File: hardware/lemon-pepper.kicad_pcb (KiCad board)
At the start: 2 copper layers, 42 x 42 mm, 124 parts, among them J101 INPUT, J201 USB_C_Receptacle_USB2.0, J301 DEBUG, M101 MOT, Q501 AO3400A, Q701 CMSA30N06T, Q702 CMSA30N06T, Q703 CMSA30N06T, SW301 RESET, SW302 USER, U201 SRV05-4, U301 STM32G431, U302 SN65HVD230, U401 MT6835, U501 FD6288, U601 MAX17504ATP+T, U602 XC6206, U801 CC6900SO-5A, U802 CC6900SO-5A, U803 CC6900SO-5A, Y301 12MHz

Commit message: try new driver
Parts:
- removed C307: 20p, Capacitor_SMD:C_0402_1005Metric
- removed C504: 470n, Capacitor_SMD:C_0805_2012Metric
- removed C603, C604: 10u, Capacitor_SMD:C_0805_2012Metric
- removed C605, C801, C802, C803: 100n, Capacitor_SMD:C_0402_1005Metric
- removed C606: 2u2, Capacitor_SMD:C_0805_2012Metric
- removed C607: 12n, Capacitor_SMD:C_0402_1005Metric
- removed C608, C609: 22uF, Capacitor_SMD:C_0805_2012Metric
- removed D503: SS210, Diode_SMD:D_SMA
- removed L601: 4u7, Inductor_SMD:L_Vishay_IHLP-4040
- removed NT601: NET TIE, NetTie:NetTie-2_SMD_Pad2.0mm
- removed Q701, Q702, Q703: CMSA30N06T, easyeda2kicad:DFN-8_L5.5-W5.2-P1.27-LS6.0-BL-EP2
- removed R303, R304, R701, R704, R705, R708, R709, R712, R713, R714, R715: 22R, Resistor_SMD:R_0402_1005Metric
- removed R305, R702, R703, R706, R707, R710, R711, R804, R805, R806: 10k, Resistor_SMD:R_0402_1005Metric
- removed R602: 100k, Resistor_SMD:R_0402_1005Metric
- removed R603: 22k, Resistor_SMD:R_0402_1005Metric
- removed R801, R802, R803: 20k, Resistor_SMD:R_0402_1005Metric
- removed SW301: RESET, matei:TS-1187A-B-A-B
- removed TP601: Vmot, TestPoint:TestPoint_Pad_D1.0mm
- removed TP602: 5V, TestPoint:TestPoint_Pad_D1.0mm
- removed TP603: 3V3, TestPoint:TestPoint_Pad_D1.0mm
- removed U602: XC6206, Package_TO_SOT_SMD:SOT-23
- removed U801, U802, U803: CC6900SO-5A, easyeda2kicad:SOP-8_L4.9-W3.9-P1.27-LS6.0-BL
- added C109: 100uF, Capacitor_SMD:CP_Elec_10x10.5, F.Cu at (86.6, 38.8)
- added C110: 100uF, Capacitor_SMD:CP_Elec_10x10.5, F.Cu at (86.6, 50.9)
- added C111: 100uF, Capacitor_SMD:CP_Elec_10x10.5, F.Cu at (86.6, 62.9)
- added C112: 100uF, Capacitor_SMD:CP_Elec_10x10.5, F.Cu at (86.6, 75.0)
- added D101: SS210, Diode_SMD:D_SMA, F.Cu at (161.9, 84.8)
- added D601: OCD, Diode_SMD:D_0603_1608Metric, F.Cu at (159.3, 87.4)
- added D602: 1N4148WS, Diode_SMD:D_SOD-323, F.Cu at (159.4, 91.9)
- added D603: 1N4148WS, Diode_SMD:D_SOD-323, F.Cu at (159.4, 89.9)
- added L501: 33u, Inductor_SMD:L_1210_3225Metric, F.Cu at (160.8, 94.5)
- added R502: 51k, Resistor_SMD:R_0402_1005Metric, F.Cu at (155.7, 96.8)
- added R503: 22k, Resistor_SMD:R_0402_1005Metric, F.Cu at (154.6, 96.8)
- added R504: 5R, Resistor_SMD:R_0603_1608Metric, F.Cu at (161.8, 79.0)
- added R505: 15k, Resistor_SMD:R_0402_1005Metric, F.Cu at (156.2, 80.0)
- added U701: ACS711KEXLT-31AB-T, easyeda2kicad:IC-SMD_ACS711KEXLT-15AB-T, F.Cu at (141.6, 78.1)
- added U702: ACS711KEXLT-31AB-T, easyeda2kicad:IC-SMD_ACS711KEXLT-15AB-T, F.Cu at (150.9, 78.1)
- added U703: ACS711KEXLT-31AB-T, easyeda2kicad:IC-SMD_ACS711KEXLT-15AB-T, F.Cu at (146.2, 78.1)
- added kibuzzard-652C57F7: G***, kibuzzard-652C57F7, F.Cu at (140.7, 89.3)
- added kibuzzard-652C580D: G***, kibuzzard-652C580D, F.Cu at (146.3, 82.3)
- added kibuzzard-652C5847: G***, kibuzzard-652C5847, F.Cu at (153.7, 88.8)
- C305: value 100n -> 20p
- C502: value 470n -> 1u; footprint Capacitor_SMD:C_0805_2012Metric -> Capacitor_SMD:C_0402_1005Metric
- C503: value 470n -> 10u
- C601: value 2u2 -> 10n; footprint Capacitor_SMD:C_0805_2012Metric -> Capacitor_SMD:C_0402_1005Metric
- C602: value 2u2 -> 220n; footprint Capacitor_SMD:C_0805_2012Metric -> Capacitor_SMD:C_0402_1005Metric
- C701, C702, C703: value 1n -> 100n
- D201: value SS210 -> 1N4148WS; footprint Diode_SMD:D_SMA -> Diode_SMD:D_SOD-323
- D501, D502: value SS210 -> BZT52C30S; footprint Diode_SMD:D_SMA -> Diode_SMD:D_SOD-323
- H101: footprint mechanical:NEMA17 -> mechanical:NEMA14
- J101: footprint easyeda2kicad:CONN-TH_4P-P0.20_XUNPU_WAFER-XH2.54-4PWB -> Connector_JST:JST_XH_B4B-XH-A_1x04_P2.50mm_Vertical
- J301: value DEBUG -> TagConnect; footprint Connector_PinHeader_1.27mm:PinHeader_2x07_P1.27mm_Vertical -> Connector:Tag-Connect_TC2030-IDC-NL_2x03_P1.27mm_Vertical
- M101: footprint easyeda2kicad:CONN-TH_4P-P0.20_XUNPU_WAFER-XH2.54-4PWB -> footprints:XH2.54 4P
- Q501: value AO3400A -> MMBT5551
- R501: value 10k -> 200k
- R601: value 20k -> 5k1
- SW302: value USER -> RESET; footprint matei:TS-1187A-B-A-B -> easyeda2kicad:KEY-SMD_4P-L2.6-W1.6-P0.80-LS3.0
- TP105: value A -> U_SENS
- TP106: value B -> A
- TP107: value Z -> B
- TP108: value U_SENS -> V_SENS
- TP109: value V_SENS -> Z
- U501: value FD6288 -> MAX15062CATA+T; footprint Package_DFN_QFN:QFN-24-1EP_4x4mm_P0.5mm_EP2.6x2.6mm -> easyeda2kicad:TDFN-8_L2.0-W2.0-P0.50-BL
- U601: value MAX17504ATP+T -> L6226QTR; footprint easyeda2kicad:QFN-20_L5.0-W5.0-P0.65-BL-EP -> easyeda2kicad:VQFN-32_L5.0-W5.0-P0.50-TL-EP
- moved FID103 106.1 mm to (162.5, 76.7)
- moved C107 102.1 mm to (154.7, 72.8), turned to 180 degrees
- moved FID102 101.6 mm to (156.9, 103.2)
- moved C104 101.4 mm to (154.7, 70.7)
- moved C105 101.3 mm to (154.7, 74.8), turned to 180 degrees
- moved C106 101.0 mm to (154.1, 91.5), turned to 90 degrees
- moved C108 99.0 mm to (152.3, 94.7), turned to 180 degrees
- moved C401 96.0 mm to (162.2, 96.7), turned to 180 degrees
- moved R103 92.7 mm to (152.1, 93.1)
- moved JP101 91.0 mm to (151.4, 91.3)
- moved C101 84.6 mm to (138.0, 70.7)
- moved C102 84.6 mm to (138.0, 72.8), turned to 180 degrees
- moved C103 84.6 mm to (138.0, 74.8)
- moved C202 83.5 mm to (141.9, 90.8)
- moved R102 82.9 mm to (141.5, 98.2), turned to 90 degrees
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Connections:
- C201 pad 1: /mcu/USB_N -> /mcu/USBD_N
- C202 pad 1: /mcu/USB_P -> /mcu/USBD_P
- C305 pad 1: /mcu/RESET -> /mcu/XIN
- C306 pad 1: /mcu/XIN -> /mcu/XOUT
- C308 pad 1: /mcu/USR_BTN -> /mcu/RESET
- C501 pad 1: /driver/DRV_PWR -> Vmot
- C502 pad 1: /driver/U_BOOTSTRAP -> Net-(U501-VCC)
- C502 pad 2: /current sense/U_IN -> GND
- C503 pad 1: /driver/V_BOOTSTRAP -> +3V3
- C503 pad 2: /current sense/V_IN -> GND
- C601 pad 1: Vmot -> Net-(D602-K)
- C601 pad 2: GNDPWR -> Net-(U601-VCP)
- C602 pad 1: Vmot -> Net-(D603-K)
- C602 pad 2: GNDPWR -> Vmot
- C701 pad 1: Net-(C701-Pad1) -> /current sense/U_SENSE
- C702 pad 1: Net-(C702-Pad1) -> /current sense/V_SENSE
- C703 pad 1: Net-(C703-Pad1) -> /current sense/W_SENSE
- D201 pad 1: +5V -> Vmot
- D501 pad 1: /driver/U_BOOTSTRAP -> Vmot
- D501 pad 2: Vmot -> Net-(D501-A)
- D502 pad 1: /driver/V_BOOTSTRAP -> Net-(D501-A)
- D502 pad 2: Vmot -> Net-(D502-A)
- J101 pad 3: /mcu/CANH -> /mcu/CANL
- J101 pad 4: /mcu/CANL -> /mcu/CANH
- J301 pad 1: unconnected-(J301-NC-Pad1) -> +3V3
- J301 pad 2: unconnected-(J301-NC-Pad2) -> /mcu/SWDIO
- J301 pad 3: +3V3 -> /mcu/RESET
- J301 pad 4: /mcu/SWDIO -> /mcu/SWCLK
- J301 pad 6: /mcu/SWCLK -> unconnected-(J301-SWO-Pad6)
- JP101 pad 1: /mcu/CANL -> /mcu/CANH
- M101 pad 2: /current sense/V_OUT -> /current sense/W_OUT
- M101 pad 3: /current sense/V_OUT -> /current sense/W_OUT
- M101 pad 4: /current sense/W_OUT -> /current sense/V_OUT
- Q501 pad 1: /driver/~{DRV_SHDN} -> Net-(Q501-B)
- Q501 pad 2: /driver/DRV_PWR -> GND
- Q501 pad 3: +5V -> Net-(Q501-C)
- R101 pad 1: GND -> /usb/UCPD_CC1
- R101 pad 2: /usb/UCPD_CC2 -> GND
- R102 pad 1: /usb/UCPD_CC1 -> GND
- R102 pad 2: GND -> /usb/UCPD_CC2
- R103 pad 1: /mcu/CANH -> /mcu/CANL
- R501 pad 1: /driver/~{DRV_SHDN} -> +3V3
- R501 pad 2: /driver/DRV_PWR -> Net-(U501-FB/VOUT)
- R601 pad 1: Net-(U601-RT) -> Net-(D601-A)
- R601 pad 2: GND -> +3V3
- SW302 pad 1: /mcu/USR_BTN -> /mcu/RESET
- TP101 pad 1: /mcu/CANH -> /mcu/CANL
- TP102 pad 1: /mcu/CANL -> /mcu/CANH
- TP103 pad 1: /mcu/USB_P -> /mcu/USBD_P
- TP104 pad 1: /mcu/USB_N -> /mcu/USBD_N
- TP105 pad 1: /encoder/A -> /current sense/U_SENSE
- TP106 pad 1: /encoder/B -> /encoder/A
- TP107 pad 1: /encoder/Z -> /encoder/B
- TP108 pad 1: /current sense/U_SENSE -> /current sense/V_SENSE
- TP109 pad 1: /current sense/V_SENSE -> /encoder/Z
- U201 pad 1: /mcu/USB_N -> /mcu/USBD_P
- U201 pad 3: /mcu/USB_P -> /mcu/USBD_N
- U201 pad 4: /mcu/USB_N -> /mcu/USBD_N
- U201 pad 5: +5V -> /usb/USB_5V
- U201 pad 6: /mcu/USB_P -> /mcu/USBD_P
- U301 pad 10: /mcu/ADC1_IN3 -> unconnected-(U301-PA2-Pad10)
- U301 pad 2: /mcu/CANL -> /mcu/CANH
- U301 pad 25: /driver/~{DRV_SHDN} -> /half bridges/ENA
- U301 pad 26: /driver/U_L -> /mcu/TIM1_CH1N
- U301 pad 27: /driver/V_L -> /mcu/TIM1_CH2N
- U301 pad 28: /driver/W_L -> /mcu/TIM1_CH3N
- U301 pad 3: /mcu/CANH -> /mcu/CANL
- U301 pad 30: /driver/U_H -> /half bridges/IN1A
- U301 pad 31: /driver/V_H -> /half bridges/IN2A
- U301 pad 32: /driver/W_H -> /half bridges/IN1B
- U301 pad 34: /mcu/USBD_N -> /mcu/USBD_P
- U301 pad 36: /mcu/SDIO -> /mcu/SWDIO
- U301 pad 39: /mcu/UART3_TX -> unconnected-(U301-PC10-Pad39)
- U301 pad 40: /mcu/UART3_RX -> unconnected-(U301-PC11-Pad40)
- U301 pad 8: /mcu/ADC1_IN1 -> unconnected-(U301-PA0-Pad8)
- U501 pad 1: /driver/U_L -> Vmot
- U501 pad 2: /driver/V_L -> Vmot
- U501 pad 3: /driver/W_L -> Net-(U501-VCC)
- U501 pad 4: /driver/DRV_PWR -> Net-(U501-FB/VOUT)
- U501 pad 5: unconnected-(U501-NC-Pad5) -> GND
- U501 pad 6: GND -> Net-(U501-VCC)
- U501 pad 7: unconnected-(U501-NC-Pad7) -> GND
- U501 pad 8: unconnected-(U501-NC-Pad8) -> Net-(U501-LX)
- U601 pad 1: Vmot -> GND
- U601 pad 10: Net-(U601-RT) -> GND
- U601 pad 11: unconnected-(U601-MODE-Pad11) -> Net-(D601-K)
- U601 pad 12: Net-(U601-VCC) -> GND
- U601 pad 13: GND -> /half bridges/IN1B
- U601 pad 14: GNDPWR -> /half bridges/IN1B
- U601 pad 15: GNDPWR -> GND
- U601 pad 16: GNDPWR -> /half bridges/ENA
- U601 pad 17: Net-(C605-Pad2) -> Net-(D603-K)
- U601 pad 18: Net-(C605-Pad2) -> GND
- U601 pad 19: Net-(C605-Pad2) -> /current sense/W_IN
- U601 pad 2: Vmot -> GND
- U601 pad 20: Net-(U601-BST) -> Vmot
- U601 pad 3: Vmot -> GND
- U601 pad 4: Vmot -> GND
- U601 pad 5: unconnected-(U601-#RESET-Pad5) -> GND
- U601 pad 6: unconnected-(U601-SYNC-Pad6) -> GND
- U601 pad 7: Net-(U601-SS) -> GND
- U601 pad 8: unconnected-(U601-CF-Pad8) -> GND
- U601 pad 9: Net-(U601-FB) -> /current sense/W_IN
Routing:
- net /mcu/SWDIO: track 0.00 -> 22.4 mm
- net /mcu/SWCLK: track 0.00 -> 21.8 mm
- net /mcu/USBD_P: track 0.00 -> 20.3 mm, vias 0 -> 2
- net +3V3: track 0.00 -> 16.6 mm, vias 0 -> 4
- net /mcu/USBD_N: track 0.00 -> 13.4 mm
- net /mcu/CANH: track 0.00 -> 13.1 mm
- net Vmot: track 0.00 -> 13.0 mm
- net /mcu/CANL: track 0.00 -> 11.6 mm
- net GND: track 0.00 -> 8.84 mm, vias 0 -> 1
- net /mcu/XIN: track 0.00 -> 6.11 mm
- net /usb/UCPD_CC2: track 0.00 -> 5.48 mm
- net Net-(D602-K): track 0.00 -> 5.06 mm
- net Net-(U601-VCP): track 0.00 -> 4.83 mm
- net /mcu/XOUT: track 0.00 -> 4.25 mm
- net /mcu/RESET: track 0.00 -> 3.68 mm
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- added copper zone on In2.Cu, net +3V3
- added copper zone on B.Cu, net GND
- added copper zone on F.Cu, net GND
- added copper zone on In1.Cu, net GND
- added copper zone on F.Cu, net Net-(U501-LX)
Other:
- board size 42 x 42 mm -> 35 x 35 mm
- copper layers 2 -> 4

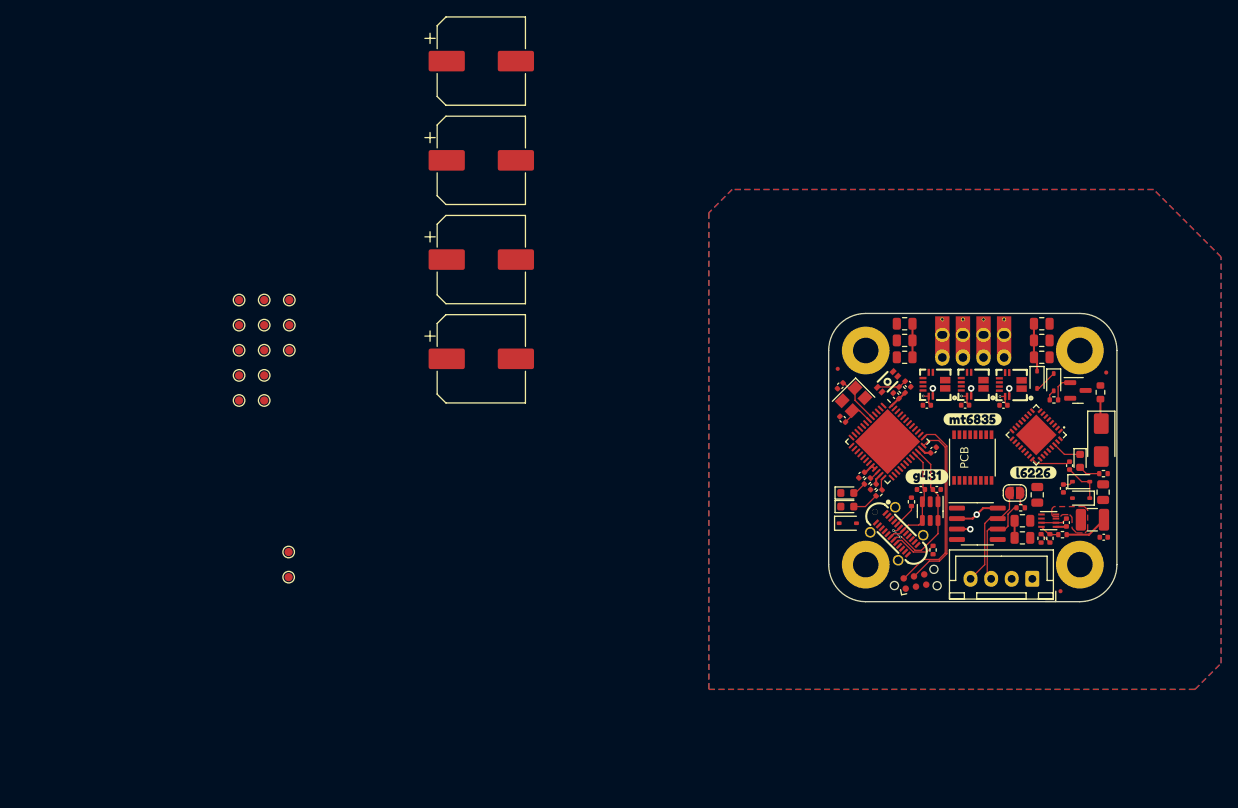
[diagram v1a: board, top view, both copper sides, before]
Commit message: change driver configuration
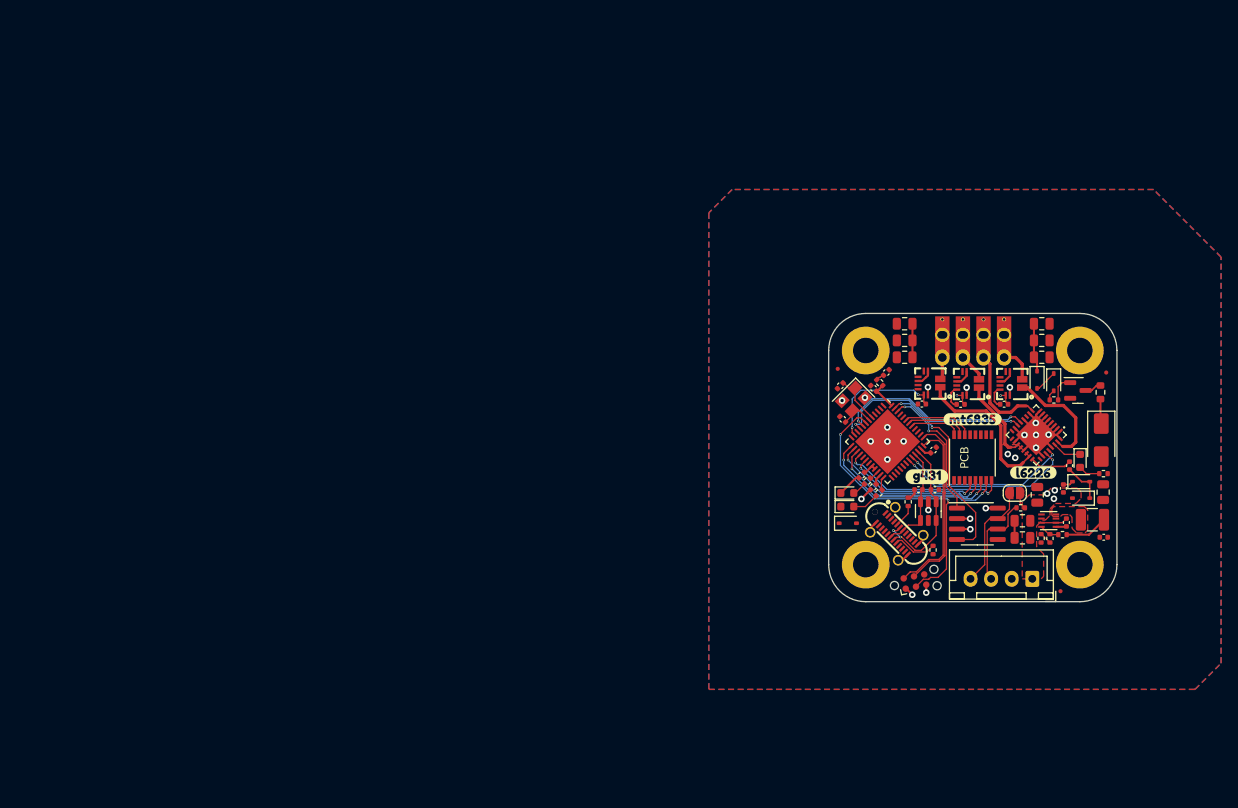
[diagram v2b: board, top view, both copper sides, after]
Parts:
- removed C109, C110, C111, C112: 100uF, Capacitor_SMD:CP_Elec_10x10.5
- removed SW302: RESET, easyeda2kicad:KEY-SMD_4P-L2.6-W1.6-P0.80-LS3.0
- removed TP101: DIR/CANH, TestPoint:TestPoint_Pad_D1.0mm
- removed TP102: STEP/CANL, TestPoint:TestPoint_Pad_D1.0mm
- removed TP103: USBP, TestPoint:TestPoint_Pad_D1.0mm
- removed TP104: USBM, TestPoint:TestPoint_Pad_D1.0mm
- removed TP105: U_SENS, TestPoint:TestPoint_Pad_D1.0mm
- removed TP106: A, TestPoint:TestPoint_Pad_D1.0mm
- removed TP107: B, TestPoint:TestPoint_Pad_D1.0mm
- removed TP108: V_SENS, TestPoint:TestPoint_Pad_D1.0mm
- removed TP109: Z, TestPoint:TestPoint_Pad_D1.0mm
- removed TP110: W_SENS, TestPoint:TestPoint_Pad_D1.0mm
- removed TP111: W, TestPoint:TestPoint_Pad_D1.0mm
- removed TP112: V, TestPoint:TestPoint_Pad_D1.0mm
- removed TP113: U, TestPoint:TestPoint_Pad_D1.0mm
- removed TP201: USB VBUS, TestPoint:TestPoint_Pad_D1.0mm
- removed TP202: USB GND, TestPoint:TestPoint_Pad_D1.0mm
- moved C308 2.97 mm to (135.8, 76.7), turned to 45 degrees
- moved C301 2.88 mm to (134.2, 78.6)
- moved R306 2.85 mm to (135.0, 77.9)
- moved C701 0.62 mm to (140.1, 80.5)
- moved U701 0.62 mm to (141.0, 77.9)
- moved U703 0.56 mm to (145.7, 78.0)
- moved C703 0.56 mm to (144.8, 80.5)
- moved R101 0.40 mm to (138.4, 92.3)
- moved C201 0.30 mm to (139.7, 90.9)
- moved C202 0.23 mm to (141.7, 90.9)
- moved U201 0.22 mm to (140.9, 93.5)
- moved C702 0.15 mm to (150.1, 80.5)
- moved U702 0.15 mm to (150.9, 78.0)
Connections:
- M101 pad 3: /current sense/W_OUT -> /half bridges/OUT1B
- U301 pad 17: /current sense/V_SENSE -> /current sense/W_SENSE
- U301 pad 18: /mcu/~{ENC_SHDN} -> /encoder/CAL_EN
- U301 pad 19: /encoder/CAL_EN -> unconnected-(U301-PB2-Pad19)
- U301 pad 26: /mcu/TIM1_CH1N -> /current sense/V_SENSE
- U301 pad 27: /mcu/TIM1_CH2N -> unconnected-(U301-PB14-Pad27)
- U301 pad 28: /mcu/TIM1_CH3N -> unconnected-(U301-PB15-Pad28)
- U301 pad 29: unconnected-(U301-PC6-Pad29) -> /mcu/MOT_EN_B
- U301 pad 30: /half bridges/IN1A -> /mcu/MOT_EN_A
- U301 pad 31: /half bridges/IN2A -> /half bridges/IN1A
- U301 pad 32: /half bridges/IN1B -> /half bridges/IN2A
- U301 pad 38: /mcu/USR_BTN -> unconnected-(U301-PA15-Pad38)
- U301 pad 41: /encoder/Z -> /encoder/A
- U301 pad 42: unconnected-(U301-PB4-Pad42) -> /encoder/B
- U301 pad 43: unconnected-(U301-PB5-Pad43) -> /encoder/Z
- U301 pad 44: /encoder/A -> unconnected-(U301-PB6-Pad44)
- U301 pad 45: /encoder/B -> unconnected-(U301-PB7-Pad45)
- U301 pad 8: unconnected-(U301-PA0-Pad8) -> /half bridges/IN1B
- U301 pad 9: /current sense/W_SENSE -> /half bridges/IN2B
- U601 pad 14: /half bridges/IN1B -> /half bridges/IN2B
- U601 pad 23: /current sense/V_IN -> /current sense/U_IN
- U601 pad 31: /current sense/U_IN -> /current sense/V_IN
- U601 pad 9: /current sense/W_IN -> /half bridges/OUT1B
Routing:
- net GND: track 8.84 -> 68.8 mm, vias 1 -> 17
- net /mcu/RESET: track 3.68 -> 36.9 mm, vias 0 -> 2
- net /mcu/CAN_RX: track 0.00 -> 24.5 mm, vias 0 -> 2
- net /half bridges/IN1B: track 0.00 -> 23.8 mm, vias 0 -> 2
- net /half bridges/IN2B: track 0.00 -> 23.8 mm, vias 0 -> 2
- net /encoder/SCK: track 0.00 -> 23.5 mm, vias 0 -> 2
- net /half bridges/IN1A: track 0.00 -> 21.6 mm, vias 0 -> 2
- net /encoder/COPI: track 0.00 -> 21.1 mm, vias 0 -> 2
- net /half bridges/IN2A: track 0.00 -> 20.7 mm, vias 0 -> 2
- net /encoder/CS: track 0.00 -> 20.7 mm, vias 0 -> 2
- net /encoder/CIPO: track 0.00 -> 20.5 mm, vias 0 -> 2
- net /current sense/U_IN: track 0.00 -> 18.3 mm
- net /mcu/CAN_TX: track 0.00 -> 17.0 mm, vias 0 -> 2
- net /encoder/CAL_EN: track 0.00 -> 17.0 mm, vias 0 -> 2
- net /current sense/V_IN: track 0.00 -> 13.6 mm
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- added copper zone on F.Cu, net Vmot
- added copper zone on In2.Cu, net Vmot

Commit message: finish layout and prod files
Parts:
- removed kibuzzard-652C5847: G***, kibuzzard-652C5847
- added R104: 0R, Resistor_SMD:R_0402_1005Metric, F.Cu at (151.2, 89.0)
- added R105: 0R, Resistor_SMD:R_0402_1005Metric, F.Cu at (150.2, 89.0)
- added kibuzzard-65305A5A: G***, kibuzzard-65305A5A, F.Cu at (154.6, 89.2)
- added kibuzzard-65306358: G***, kibuzzard-65306358, F.Cu at (149.3, 99.1)
- moved FID102 27.5 mm to (130.2, 96.8)
- moved R101 6.61 mm to (142.1, 97.8)
- moved R102 6.50 mm to (138.7, 92.3)
- moved J301 0.25 mm to (139.1, 102.2)
- turned D201 to 180 degrees
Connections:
- R101 pad 1: /usb/UCPD_CC1 -> GND
- R101 pad 2: GND -> /usb/UCPD_CC2
- R102 pad 1: GND -> /usb/UCPD_CC1
- R102 pad 2: /usb/UCPD_CC2 -> GND
- U301 pad 2: /mcu/CANH -> unconnected-(U301-PC13-Pad2)
- U301 pad 27: unconnected-(U301-PB14-Pad27) -> /mcu/STEP
- U301 pad 28: unconnected-(U301-PB15-Pad28) -> /mcu/DIR
- U301 pad 3: /mcu/CANL -> unconnected-(U301-PC14-Pad3)
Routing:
- net GND: track 68.8 -> 100.3 mm, vias 17 -> 39
- net /half bridges/ENA: track 0.00 -> 29.1 mm, vias 0 -> 3
- net Vmot: track 13.0 -> 39.3 mm, vias 5 -> 15
- net /current sense/V_SENSE: track 1.79 -> 20.6 mm, vias 1 -> 4
- net /current sense/W_SENSE: track 1.88 -> 19.9 mm, vias 1 -> 4
- net /mcu/DIR: track 0.00 -> 16.0 mm, vias 0 -> 2
- net /mcu/STEP: track 0.00 -> 14.9 mm, vias 0 -> 2
- net +3V3: track 19.3 -> 34.2 mm, vias 5 -> 14
- net Net-(D603-K): track 1.24 -> 12.7 mm, vias 0 -> 2
- net Net-(D601-K): track 3.58 -> 14.8 mm, vias 0 -> 2
- net /mcu/RESET: track 36.9 -> 47.6 mm, vias 2 -> 3
- net /usb/USB_5V: track 0.00 -> 7.56 mm, vias 0 -> 6
- net /mcu/CANL: track 11.6 -> 18.4 mm
- net /half bridges/IN2A: track 20.7 -> 25.8 mm
- net /half bridges/IN1A: track 21.6 -> 25.0 mm
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- added copper zone on B.Cu, net /usb/USB_5V
- added copper zone on B.Cu, net Vmot

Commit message: board logo
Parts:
- added G***: LOGO, LOGO, B.Cu at (145.6, 85.8)
- kibuzzard-65306358: moved to B.Cu
- moved kibuzzard-65306358 0.93 mm to (149.8, 99.8), turned to 180 degrees

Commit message: update fab files
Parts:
- moved kibuzzard-65306358 5.49 mm to (144.5, 98.6)
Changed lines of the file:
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@@
   )
   (footprint "kibuzzard-65306358" (layer "B.Cu")
-    (at 149.85 99.85 180)
+    (at 144.5 98.625 180)
     (descr "Generated with KiBuzzard")
     (tags "kb_params=eyJBbGlnbm1lbnRDaG9pY2UiOiAiQ2VudGVyIiwgIkNhcExlZnRDaG9pY2UiOiAiKCIsICJDYXBSaWdodENob2ljZSI6ICIpIiwgIkZvbnRDb21ib0JveCI6ICJGcmVkb2thT25lIiwgIkhlaWdodEN0cmwiOiAiMSIsICJMYXllckNvbWJvQm94IjogIkYuU2lsa1MiLCAiTXVsdGlMaW5lVGV4dCI6ICJtYXRlaWpvcmRhY2hlIiwgIlBhZGRpbmdCb3R0b21DdHJsIjogIjIiLCAiUGFkZGluZ0xlZnRDdHJsIjogIjAiLCAiUGFkZGluZ1JpZ2h0Q3RybCI6ICIwIiwgIlBhZGRpbmdUb3BDdHJsIjogIjIiLCAiV2lkdGhDdHJsIjogIjIifQ==")

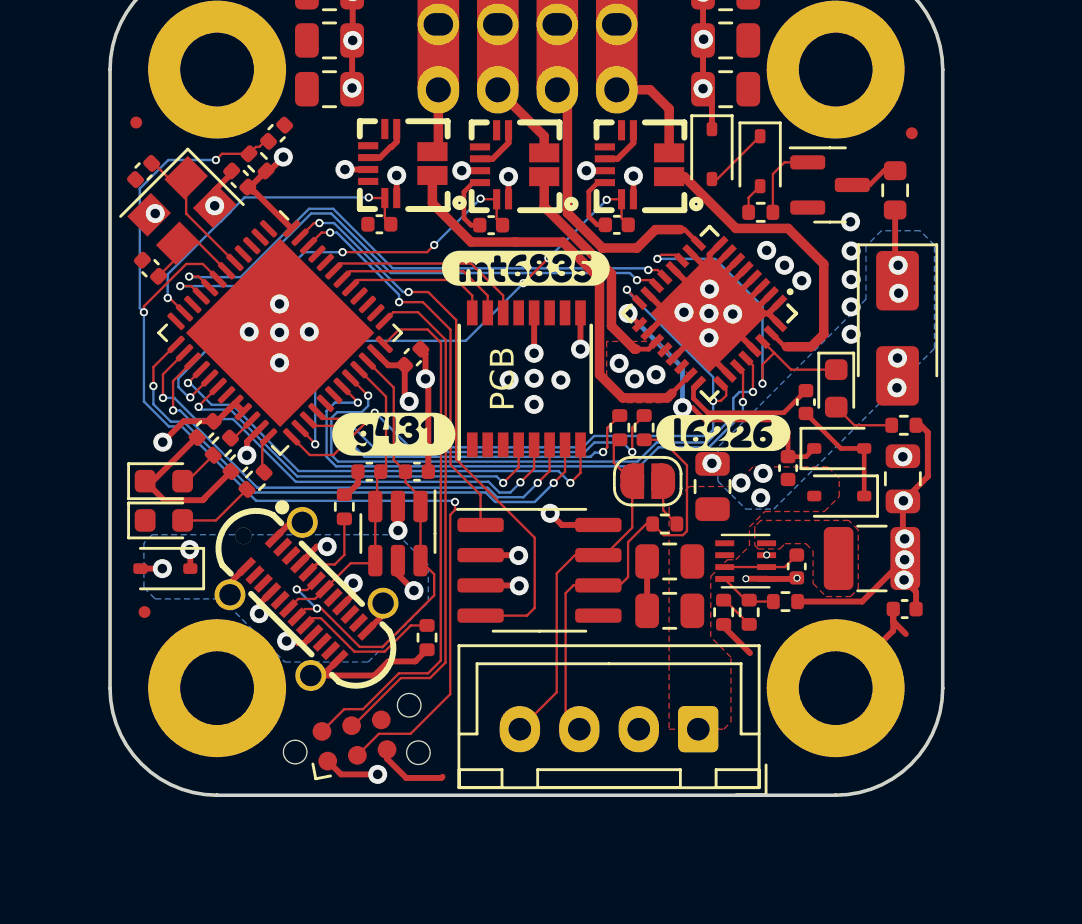
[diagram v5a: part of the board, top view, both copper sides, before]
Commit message: rework power plane
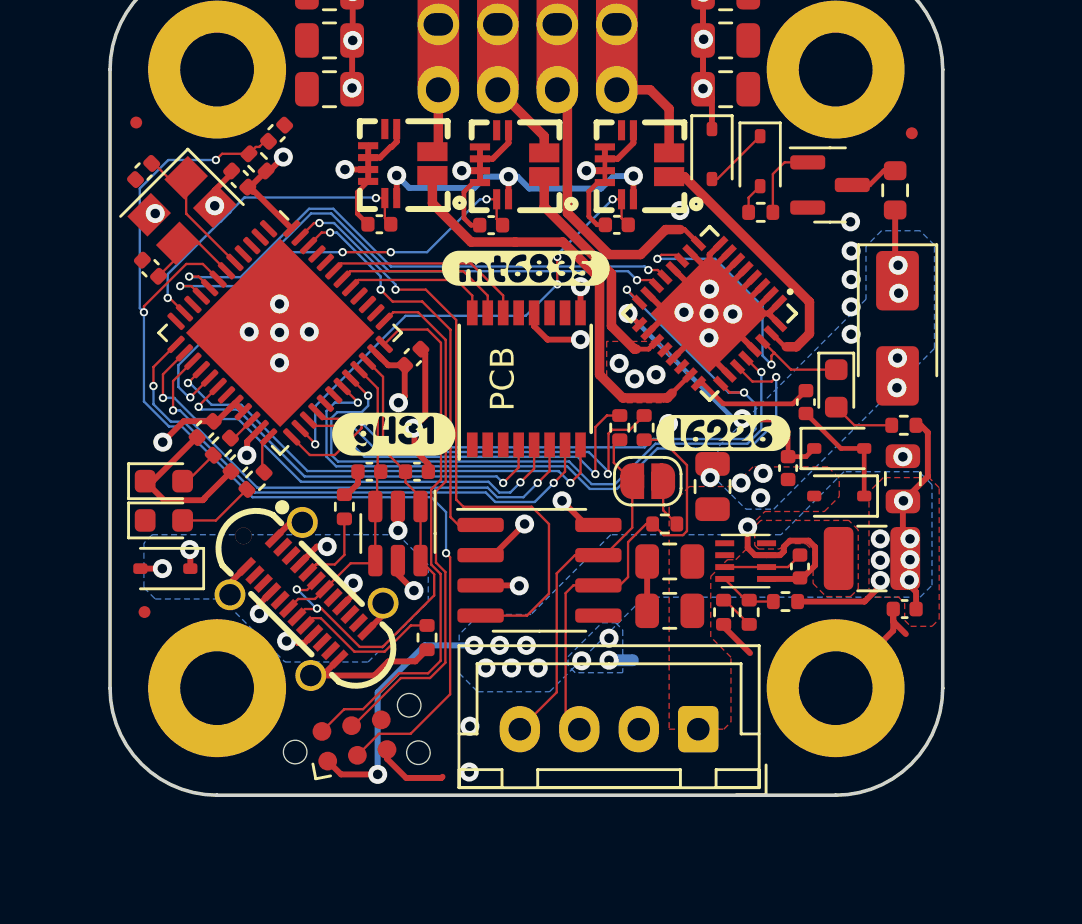
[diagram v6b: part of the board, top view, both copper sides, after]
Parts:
- added NT701: NetTie_2, NetTie:NetTie-2_SMD_Pad0.5mm, B.Cu at (150.3, 98.8)
- moved C502 0.14 mm to (157.8, 94.9)
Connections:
- C701 pad 2: GND -> GNDA
- C702 pad 2: GND -> GNDA
- C703 pad 2: GND -> GNDA
- U401 pad 12: GND -> GNDA
- U701 pad 10: GND -> GNDA
- U701 pad 5: GND -> GNDA
- U701 pad 7: GND -> GNDA
- U701 pad 8: GND -> GNDA
- U701 pad 9: GND -> GNDA
- U702 pad 10: GND -> GNDA
- U702 pad 5: GND -> GNDA
- U702 pad 7: GND -> GNDA
- U702 pad 8: GND -> GNDA
- U702 pad 9: GND -> GNDA
- U703 pad 10: GND -> GNDA
- U703 pad 5: GND -> GNDA
- U703 pad 7: GND -> GNDA
- U703 pad 8: GND -> GNDA
- U703 pad 9: GND -> GNDA
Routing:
- net +3V3: track 34.2 -> 82.0 mm, vias 14 -> 23
- net GNDA: track 0.00 -> 24.1 mm, vias 0 -> 7
- net GND: track 100.3 -> 91.0 mm, vias 39 -> 30
- net /half bridges/IN1A: track 25.0 -> 28.8 mm
- net /half bridges/ENA: track 29.1 -> 31.7 mm
- net /mcu/CAN_RX: track 24.4 -> 26.7 mm
- net /current sense/V_IN: track 13.6 -> 11.5 mm
- net /half bridges/IN2A: track 25.8 -> 27.6 mm
- net Net-(D601-K): track 14.8 -> 13.2 mm
- net /mcu/STEP: track 14.9 -> 16.2 mm
- net Net-(D603-K): track 12.7 -> 11.8 mm
- net Net-(U601-VCP): track 6.08 -> 5.10 mm
- net /mcu/DIR: track 16.0 -> 16.9 mm
- net Vmot: track 39.3 -> 38.5 mm
- net /mcu/CAN_TX: track 16.8 -> 17.5 mm
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- added copper zone on B.Cu, net +3V3
- added copper zone on F.Cu, net +3V3
- added copper zone on In2.Cu, net GND
- added copper zone on B.Cu, net GNDA
- added copper zone on In2.Cu, net GNDA
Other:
- board text added: "PCB3D_BR_LEMON"
- board text added: "PCB3D_TL_LEMON"
